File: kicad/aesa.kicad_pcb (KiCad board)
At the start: 4 copper layers, 192 x 301 mm, 2064 parts, among them J9501 12 V in (5.5x2.1), J9502 TX power (shunt), J9901 EX_IO1 (AXU3EGB J15), J9902 EX_IO2 (AXU3EGB J16), U1001 OPA1678IDR, U101 OPA1678IDR, U10101 74HCT595D, U10102 UCC27524DR, U10103 UCC27524DR, U10201 74HCT595D, U10202 UCC27524DR, U10203 UCC27524DR, U10301 74HCT595D, U10302 UCC27524DR, U10303 UCC27524DR, U10401 74HCT595D, U10402 UCC27524DR, U10403 UCC27524DR, U10501 74HCT595D, U10502 UCC27524DR, U10503 UCC27524DR, U10601 74HCT595D, U10602 UCC27524DR, U10603 UCC27524DR, U10701 74HCT595D, U10702 UCC27524DR, U10703 UCC27524DR, U10801 74HCT595D, U10802 UCC27524DR, U10803 UCC27524DR, U10901 74HCT595D, U10902 UCC27524DR, U10903 UCC27524DR, U11001 74HCT595D, U11002 UCC27524DR, U11003 UCC27524DR, U1101 OPA1678IDR, U11101 74HCT595D, U11102 UCC27524DR, U11103 UCC27524DR, U11201 74HCT595D, U11202 UCC27524DR, U11203 UCC27524DR, U11301 74HCT595D, U11302 UCC27524DR, U11303 UCC27524DR, U11401 74HCT595D, U11402 UCC27524DR, U11403 UCC27524DR, U11501 74HCT595D, U11502 UCC27524DR, U11503 UCC27524DR, U11601 74HCT595D, U11602 UCC27524DR, U11603 UCC27524DR, U1201 OPA1678IDR, U12101 74AHCT1G125, U12201 74AHCT1G125, U12301 74AHCT1G125, U12401 74AHCT1G125, U1301 OPA1678IDR, U13101 74LVC2G34, U13201 74LVC2G34, U13301 74LVC2G34, U13401 74LVC2G34, U13501 74LVC2G34, U13601 74LVC2G34, U13701 74LVC2G34, U13801 74LVC2G34, U13901 74LVC2G34, U1401 OPA1678IDR, U1501 OPA1678IDR, U1601 OPA1678IDR, U1701 OPA1678IDR, U1801 OPA1678IDR, U1901 OPA1678IDR, U2001 OPA1678IDR, U201 OPA1678IDR, U2101 OPA1678IDR, U2201 OPA1678IDR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

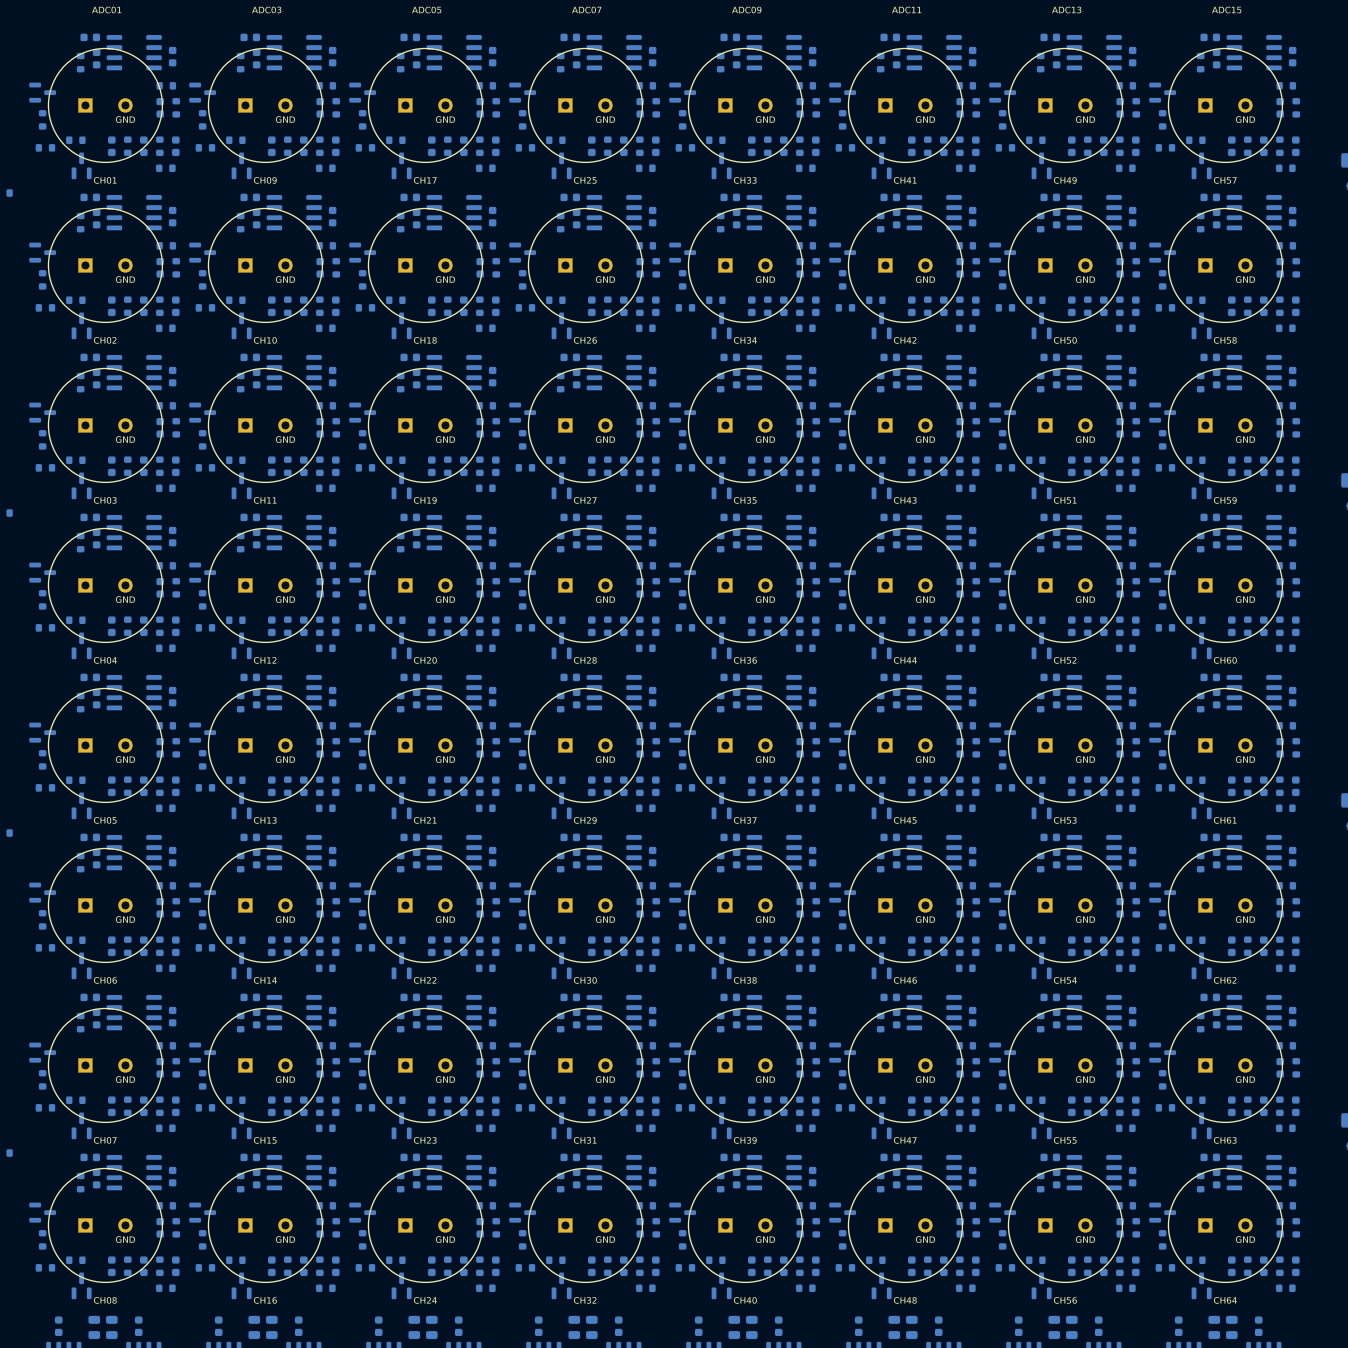
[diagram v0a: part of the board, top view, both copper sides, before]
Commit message: Transducer: Same Sky CUSP-TR80-15-2500-TH instead of CUSA-TR65 (about $122 less per board)
- Ø9.8 mm 40 kHz transceiver, 105 dB SPL, 0.2-15 m, 1.6 ms ring-down, 2.0 nF; $1.65 (Future,
  DigiKey second source); not sealed (indoor, behind the waveguide)
- new footprint aesa:CUSP-TR80 (5.0 mm pin pitch, Ø2 mm pads, Ø0.9 mm holes, '+' = pad 1);
  CUSA-TR65 footprint removed; soldering keep-out follows the larger pads
- simulation model CUSP_TR80 (C0 2.0 nF; Rm 3 k and the 1 m echo level kept as assumptions):
  all 10 simulations pass
- BOM total $326 per board (was $444); datasheet library, checks, brief and README updated;
  board re-placed, DRC 0 violations
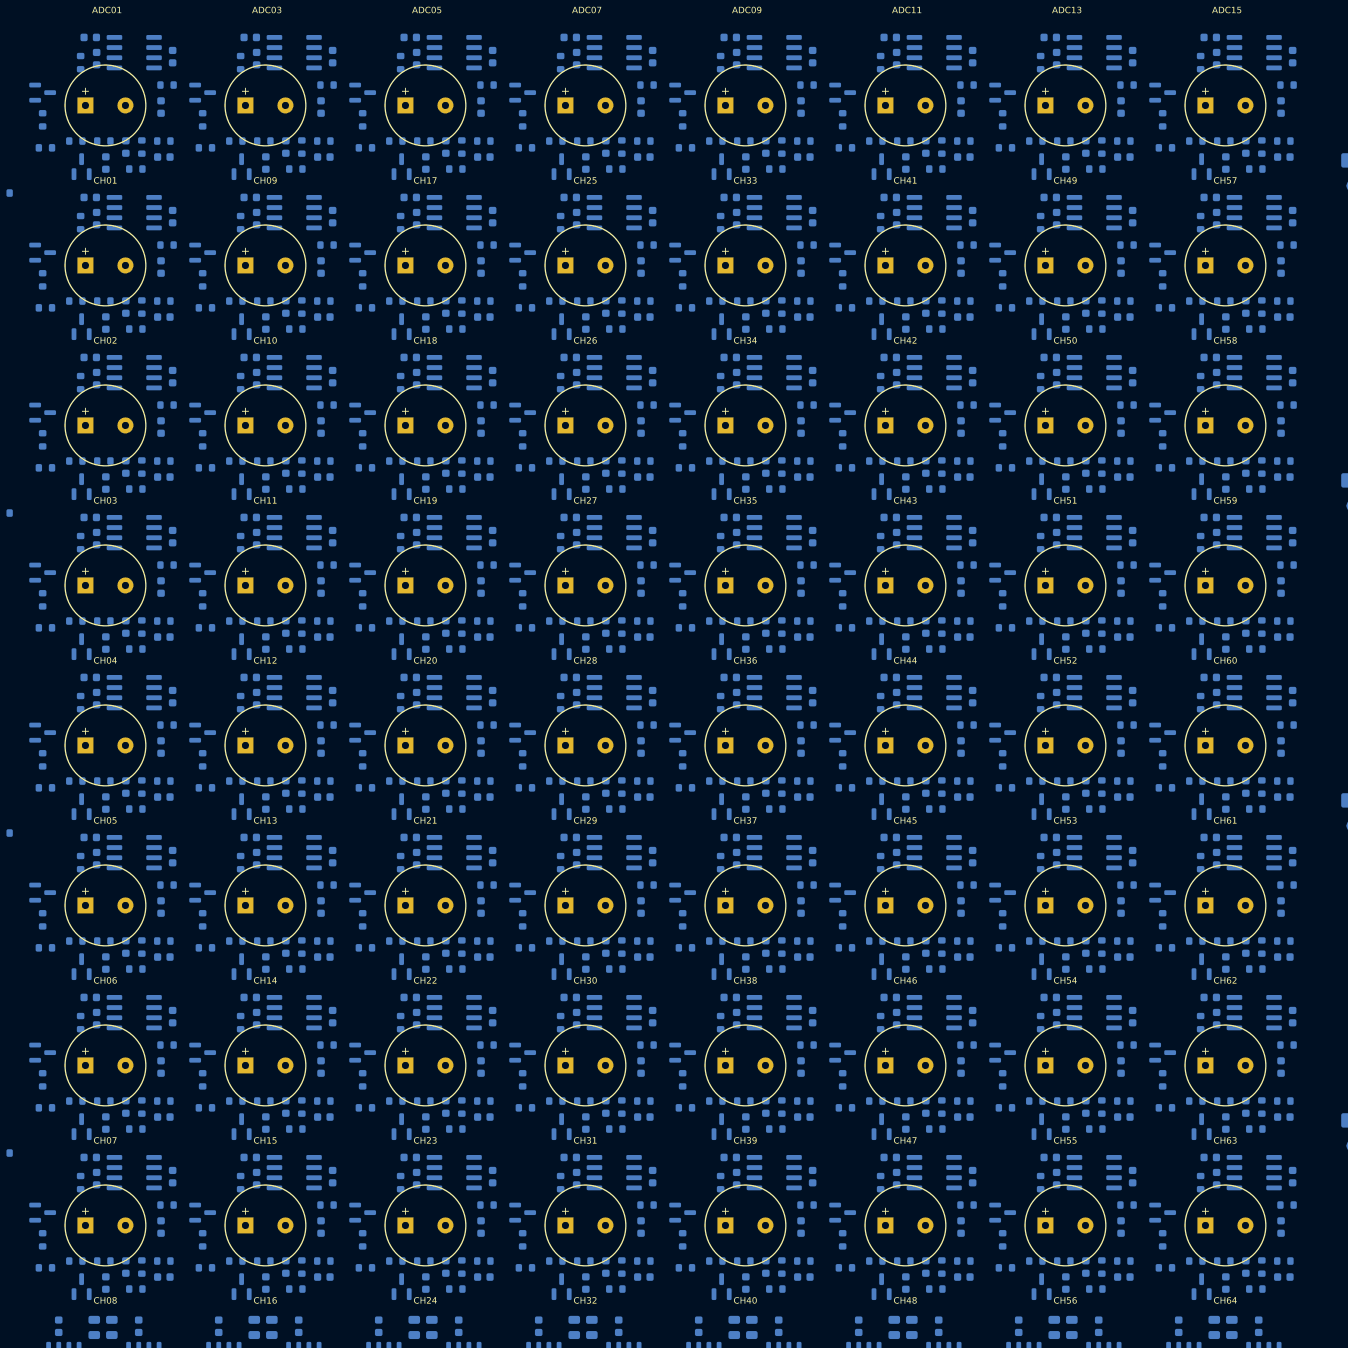
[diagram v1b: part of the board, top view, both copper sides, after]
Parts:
- LS1001, LS101, LS1101, LS1201, LS1301, LS1401, LS1501, LS1601, LS1701, LS1801, LS1901, LS2001, LS201, LS2101, LS2201, LS2301, LS2401, LS2501, LS2601, LS2701, LS2801, LS2901, LS3001, LS301, LS3101, LS3201, LS3301, LS3401, LS3501, LS3601, LS3701, LS3801, LS3901, LS4001, LS401, LS4101, LS4201, LS4301, LS4401, LS4501, LS4601, LS4701, LS4801, LS4901, LS5001, LS501, LS5101, LS5201, LS5301, LS5401, LS5501, LS5601, LS5701, LS5801, LS5901, LS6001, LS601, LS6101, LS6201, LS6301, LS6401, LS701, LS801, LS901: value CUSA-TR65-065-2200-TH68 -> CUSP-TR80-15-2500-TH; footprint CUSA-TR65 -> CUSP-TR80
- moved R209 4.43 mm to (33.3, 97.5), turned to 0 degrees
- moved R309 4.43 mm to (33.3, 117.5), turned to 0 degrees
- moved R409 4.43 mm to (33.3, 137.4), turned to 0 degrees
- moved R509 4.43 mm to (33.3, 157.4), turned to 0 degrees
- moved R609 4.43 mm to (33.3, 177.4), turned to 0 degrees
- moved R709 4.43 mm to (33.3, 197.4), turned to 0 degrees
- moved R809 4.43 mm to (33.3, 217.4), turned to 0 degrees
- moved R1009 4.43 mm to (53.3, 97.5), turned to 0 degrees
- moved R109 4.43 mm to (33.3, 77.5), turned to 0 degrees
- moved R1109 4.43 mm to (53.3, 117.5), turned to 0 degrees
- moved R1709 4.43 mm to (73.3, 77.5), turned to 0 degrees
- moved R1809 4.43 mm to (73.3, 97.5), turned to 0 degrees
- moved R1909 4.43 mm to (73.3, 117.5), turned to 0 degrees
- moved R2509 4.43 mm to (93.3, 77.5), turned to 0 degrees
- moved R2609 4.43 mm to (93.3, 97.5), turned to 0 degrees
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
